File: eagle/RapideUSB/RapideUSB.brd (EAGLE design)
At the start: 50 x 50 mm, 36 parts, among them Y1 12-20MHz

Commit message: Board finished and ready to send to production.
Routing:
- net D3: track 62.4 -> 61.7 mm
- net GND: vias 19 -> 21
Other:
- board text added: "D+"
- board text added: "D+=D2"
- board text added: "D-"
- board text added: "D-=D4"
- board text added: "RapideUSB"
- board text added: "RapideUSB v1.0 Jan2015"
- board text added: "USB"
- board text added: "http://kalshagar.wikispaces.com/RapideUSB"
- board text removed: "C8"
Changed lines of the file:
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@@
 <text x="1.11125" y="42.06875" size="0.8128" layer="150" rot="R90">GND</text>
 <text x="1.11125" y="39.37" size="0.8128" layer="150" rot="R90">VCC</text>
-<text x="1.11125" y="30.95625" size="0.8128" layer="150" rot="R90">Cut  ok</text>
-<text x="50.00625" y="30.95625" size="0.8128" layer="150" rot="R90">Cut  ok</text>
+<text x="1.11125" y="30.95625" size="0.8128" layer="150" rot="R90">Cut ok</text>
+<text x="49.8475" y="30.95625" size="0.8128" layer="150" rot="R90">Cut ok</text>
 <rectangle x1="0" y1="17.78" x2="3.81" y2="20.32" layer="150"/>
 <text x="4.1275" y="7.46125" size="1.27" layer="150">ATtiny2313</text>
@@
 <text x="41.5925" y="15.71625" size="0.8128" layer="150">R2</text>
 <text x="41.5925" y="17.78" size="0.8128" layer="150">R3</text>
-<text x="1.27" y="25.4" size="1.27" layer="150">D0</text>
-<text x="26.67" y="25.4" size="1.27" layer="150">B328</text>
+<text x="1.27" y="25.7175" size="1.016" layer="150">D0</text>
+<text x="26.67" y="25.7175" size="1.016" layer="150">B328</text>
 <text x="23.65375" y="20.0025" size="0.8128" layer="150" rot="SR180">B2313</text>
-<text x="48.26" y="23.1775" size="0.8128" layer="150">C8</text>
 <text x="27.6225" y="21.74875" size="0.8128" layer="150">C0</text>
 <wire x1="20.32" y1="19.685" x2="17.145" y2="19.685" width="0.1524" layer="150"/>
@@
 <wire x1="33.655" y1="25.7175" x2="34.44875" y2="26.035" width="0.1524" layer="150"/>
 <text x="35.8775" y="16.35125" size="0.8128" layer="150">1.5k</text>
+<text x="48.73625" y="25.55875" size="1.27" layer="52" rot="MR0">http://kalshagar.wikispaces.com/RapideUSB</text>
+<text x="13.49375" y="25.55875" size="1.4224" layer="150">RapideUSB</text>
+<wire x1="20.32" y1="11.43" x2="16.51" y2="17.78" width="0.6096" layer="52"/>
+<wire x1="16.51" y1="17.78" x2="16.51" y2="11.43" width="0.6096" layer="52"/>
+<wire x1="16.51" y1="11.43" x2="16.51" y2="3.81" width="0.6096" layer="52"/>
+<wire x1="16.51" y1="3.81" x2="12.7" y2="11.43" width="0.6096" layer="52"/>
+<wire x1="16.51" y1="11.43" x2="19.05" y2="11.43" width="0.6096" layer="52"/>
+<wire x1="33.02" y1="6.35" x2="35.56" y2="10.16" width="0.6096" layer="150"/>
+<wire x1="35.56" y1="10.16" x2="35.56" y2="6.35" width="0.6096" layer="150"/>
+<wire x1="35.56" y1="6.35" x2="35.56" y2="2.54" width="0.6096" layer="150"/>
+<wire x1="35.56" y1="2.54" x2="38.1" y2="6.35" width="0.6096" layer="150"/>
+<wire x1="35.56" y1="6.35" x2="34.29" y2="6.35" width="0.6096" layer="150"/>
+<text x="14.2875" y="11.43" size="0.6096" layer="150" rot="R90">D+=D2</text>
+<text x="16.51" y="11.58875" size="0.6096" layer="150" rot="R90">D-=D4</text>
+<text x="13.0175" y="18.415" size="0.6096" layer="150">D+</text>
+<text x="15.5575" y="18.415" size="0.6096" layer="150">D-</text>
+<wire x1="3.81" y1="24.765" x2="3.81" y2="23.495" width="0.254" layer="150"/>
+<wire x1="21.59" y1="22.225" x2="21.59" y2="20.955" width="0.254" layer="150"/>
+<wire x1="29.21" y1="24.765" x2="29.21" y2="23.495" width="0.254" layer="150"/>
+<wire x1="31.75" y1="22.225" x2="31.75" y2="20.955" width="0.254" layer="150"/>
+<text x="20.0025" y="0.3175" size="0.6096" layer="150">RapideUSB v1.0 Jan2015</text>
+<text x="47.78375" y="8.41375" size="1.27" layer="150" rot="R90">USB</text>
 </plain>
 <attributes>
@@
 <wire x1="43.18" y1="12.54125" x2="44.1325" y2="10.795" width="0.4064" layer="1"/>
 <contactref element="C5" pad="2"/>
+<via x="3.81" y="5.08" extent="1-16" drill="0.5" shape="octagon"/>
+<via x="22.225" y="6.6675" extent="1-16" drill="0.5" shape="octagon"/>
 </signal>
 <signal name="B7">
@@
 <wire x1="30.1625" y1="3.4925" x2="31.115" y2="3.4925" width="0.1524" layer="16"/>
 <wire x1="30.1625" y1="7.3025" x2="30.1625" y2="3.4925" width="0.1524" layer="1"/>
-<wire x1="22.5425" y1="7.3025" x2="30.1625" y2="7.3025" width="0.1524" layer="1"/>
-<wire x1="20.32" y1="4.1275" x2="22.5425" y2="7.3025" width="0.1524" layer="1"/>
+<wire x1="25.0825" y1="7.3025" x2="30.1625" y2="7.3025" width="0.1524" layer="1"/>
+<wire x1="20.32" y1="4.1275" x2="25.0825" y2="7.3025" width="0.1524" layer="1"/>
 <wire x1="20.32" y1="2.54" x2="20.32" y2="4.1275" width="0.1524" layer="1"/>
 <wire x1="31.115" y1="3.4925" x2="31.2674" y2="3.55" width="0.1524" layer="16"/>

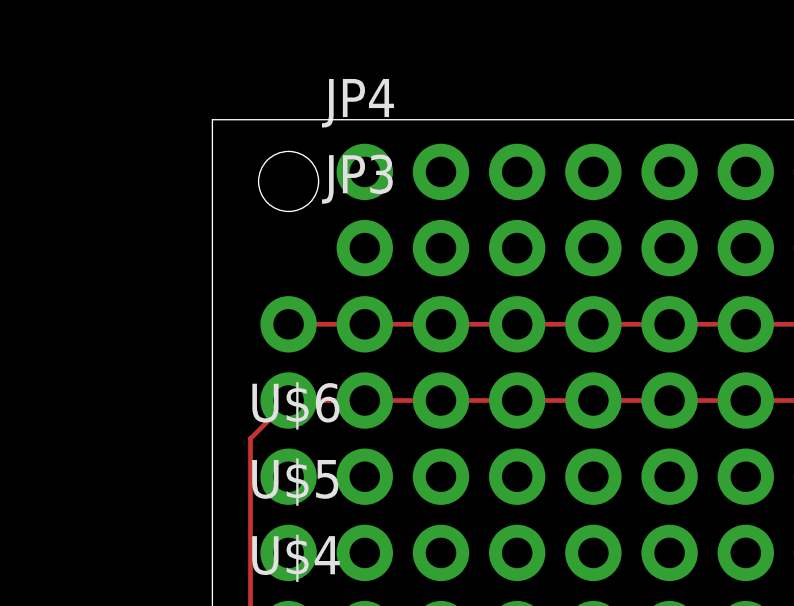
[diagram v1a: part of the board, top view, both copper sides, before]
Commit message: v1.1: fixed the power pin top-vias pins and added a nice V-USB logo.
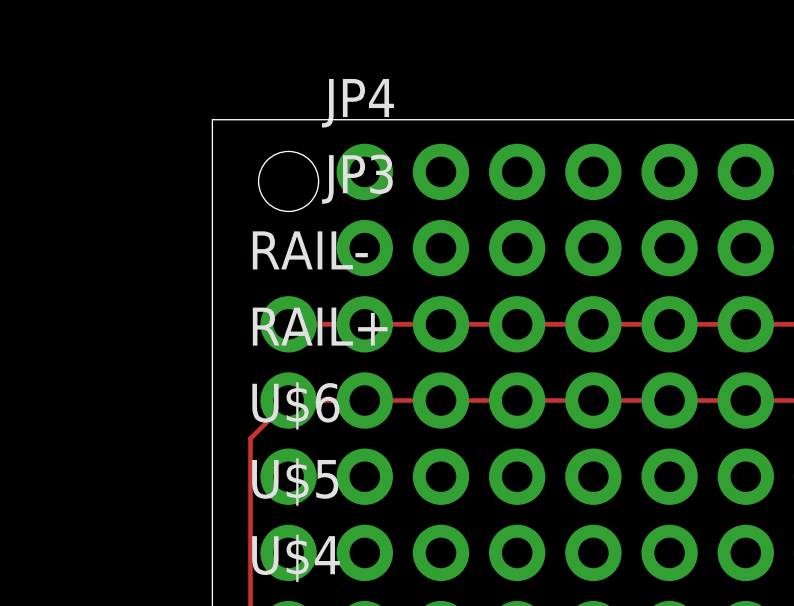
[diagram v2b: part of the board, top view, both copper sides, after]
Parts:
- added U$1: (no value), kalshagar-images:VUSB_LOGO
- RAIL+, RAIL-: value M17KIT -> M17NOSILK; device SparkFun-Connectors:1X17_NO_SILK_KIT -> SparkFun-Connectors:1X17_NO_SILK
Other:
- board text added: "RapideUSB v1.1 Jan2015"
- board text removed: "RapideUSB v1.0 Jan2015"
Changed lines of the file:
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@@
 <wire x1="29.21" y1="24.765" x2="29.21" y2="23.495" width="0.254" layer="150"/>
 <wire x1="31.75" y1="22.225" x2="31.75" y2="20.955" width="0.254" layer="150"/>
-<text x="20.0025" y="0.3175" size="0.6096" layer="150">RapideUSB v1.0 Jan2015</text>
+<text x="20.0025" y="0.3175" size="0.6096" layer="150">RapideUSB v1.1 Jan2015</text>
 <text x="47.78375" y="8.41375" size="1.27" layer="150" rot="R90">USB</text>
 </plain>
@@
 <element name="C3" library="resistor" package="C025-024X044" value="1uF" x="10.16" y="12.7"/>
 <element name="C4" library="resistor" package="E2-5" value="10uF+" x="10.16" y="16.51" rot="R90"/>
-<element name="RAIL+" library="SparkFun-Connectors" package="1X17_NO_SILK_KIT" value="M17KIT" x="2.54" y="40.64"/>
-<element name="RAIL-" library="SparkFun-Connectors" package="1X17_NO_SILK_KIT" value="M17KIT" x="2.54" y="43.18"/>
+<element name="RAIL+" library="SparkFun-Connectors" package="1X17_NO_SILK" value="M17NOSILK" x="2.54" y="40.64"/>
+<element name="RAIL-" library="SparkFun-Connectors" package="1X17_NO_SILK" value="M17NOSILK" x="2.54" y="43.18"/>
 <element name="U$2" library="SparkFun-Connectors" package="1X19_NO_SILK" value="M191X19_NO_SILK" x="2.54" y="27.94"/>
 <element name="U$3" library="SparkFun-Connectors" package="1X19_NO_SILK" value="M191X19_NO_SILK" x="2.54" y="30.48"/>
@@
 <element name="JP4" library="SparkFun-Connectors" package="1X16_NO_SILK" value="M161X16_NO_SILK" x="5.08" y="48.26"/>
 <element name="C5" library="resistor" package="C025-024X044" value="1uF" x="42.8625" y="1.74625" rot="R180"/>
+<element name="U$1" library="kalshagar-images" package="VUSB_LOGO" value="" x="32.385" y="12.3825"/>
 </elements>
 <signals>

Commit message: I made a mistake and PC2 is in fact not connected
Since I won't make another batch and that routing that one wire looks
like a nightmare, I just remove it from schematics to avoid confusion
later. A good lesson learnt.
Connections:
- removed net N$7: UC2.25
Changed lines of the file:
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@@
 <?xml version="1.0" encoding="utf-8"?>
 <!DOCTYPE eagle SYSTEM "eagle.dtd">
-<eagle version="6.3">
+<eagle version="7.2.0">
 <drawing>
 <settings>
@@
 <layer number="56" name="wert" color="7" fill="1" visible="no" active="no"/>
 <layer number="57" name="tCAD" color="7" fill="1" visible="no" active="no"/>
-<layer number="90" name="Modules" color="5" fill="1" visible="yes" active="yes"/>
+<layer number="90" name="Modules" color="5" fill="1" visible="no" active="no"/>
 <layer number="91" name="Nets" color="2" fill="1" visible="no" active="no"/>
 <layer number="92" name="Busses" color="1" fill="1" visible="no" active="no"/>
@@
 <pass name="Default">
 <param name="RoutingGrid" value="6.25mil"/>
+<param name="AutoGrid" value="1"/>
+<param name="Efforts" value="0"/>
+<param name="TopRouterVariant" value="1"/>
 <param name="tpViaShape" value="round"/>
 <param name="PrefDir.1" value="|"/>
@@
 <via x="35.2425" y="20.16125" extent="1-16" drill="0.3048"/>
 </signal>
-<signal name="N$7">
-<contactref element="UC2" pad="25"/>
-</signal>
 <signal name="N$8">

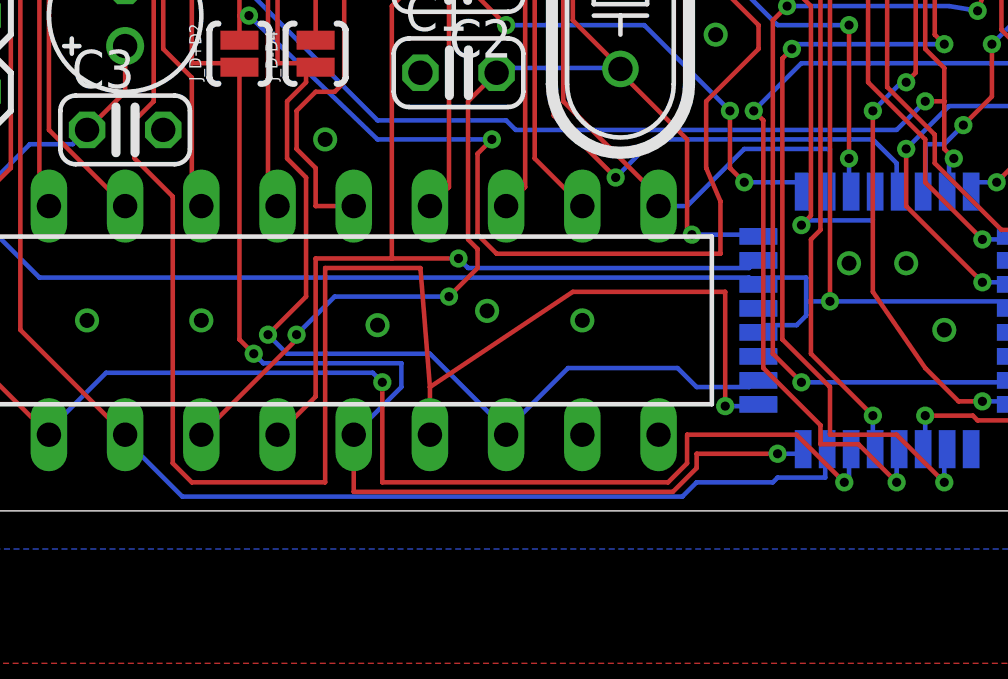
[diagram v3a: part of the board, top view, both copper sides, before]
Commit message: Bugfix: PD5 was unconnected on 2313
Added missing wire on board v1.2.
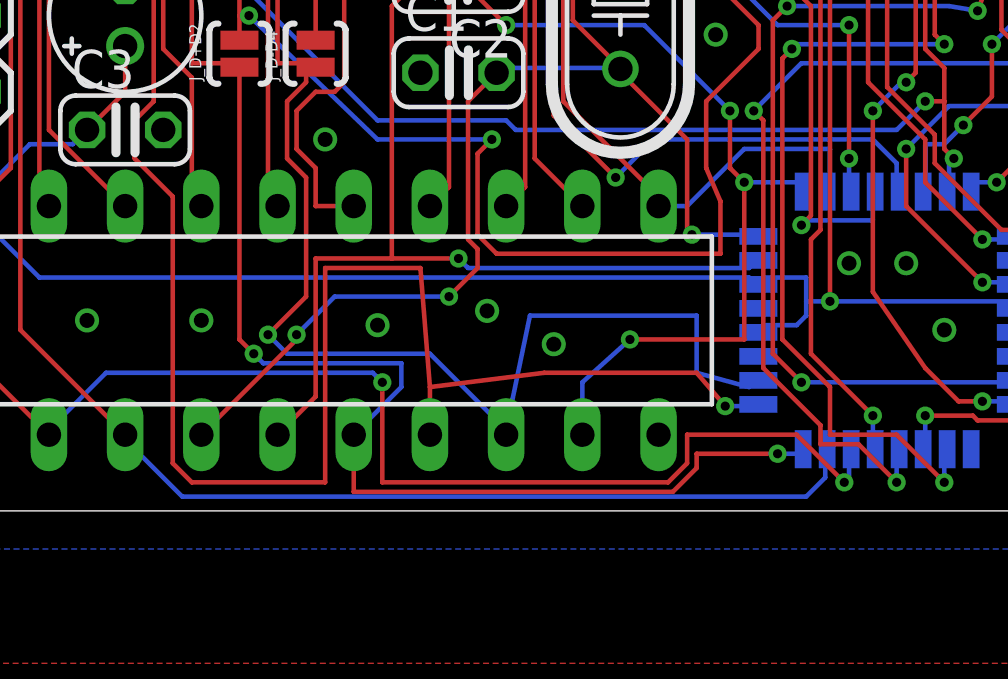
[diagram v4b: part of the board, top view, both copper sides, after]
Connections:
- removed net N$16: PORTD.6, UC2.9
- net D5: now also PORTD.6, UC2.9
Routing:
- net D5: track 0.00 -> 39.1 mm, vias 0 -> 4
- net N$16: track 26.2 -> 0.00 mm, vias 3 -> 0
- net D3: track 61.7 -> 57.5 mm
- net D4: track 41.1 -> 45.1 mm
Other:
- board text added: "RapideUSB v1.2 Dec2016"
- board text added: "http://electrogeek.cc/RapideUSB"
- board text removed: "RapideUSB v1.1 Jan2015"
- board text removed: "http://kalshagar.wikispaces.com/RapideUSB"
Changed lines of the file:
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@@
 <wire x1="33.655" y1="25.7175" x2="34.44875" y2="26.035" width="0.1524" layer="150"/>
 <text x="35.8775" y="16.35125" size="0.8128" layer="150">1.5k</text>
-<text x="48.73625" y="25.55875" size="1.27" layer="52" rot="MR0">http://kalshagar.wikispaces.com/RapideUSB</text>
+<text x="48.73625" y="25.55875" size="1.27" layer="52" rot="MR0">http://electrogeek.cc/RapideUSB</text>
 <text x="13.49375" y="25.55875" size="1.4224" layer="150">RapideUSB</text>
 <wire x1="20.32" y1="11.43" x2="16.51" y2="17.78" width="0.6096" layer="52"/>
@@
 <wire x1="29.21" y1="24.765" x2="29.21" y2="23.495" width="0.254" layer="150"/>
 <wire x1="31.75" y1="22.225" x2="31.75" y2="20.955" width="0.254" layer="150"/>
-<text x="20.0025" y="0.3175" size="0.6096" layer="150">RapideUSB v1.1 Jan2015</text>
+<text x="20.0025" y="0.3175" size="0.6096" layer="150">RapideUSB v1.2 Dec2016</text>
 <text x="47.78375" y="8.41375" size="1.27" layer="150" rot="R90">USB</text>
 </plain>
@@
 <via x="16.8275" y="12.3825" extent="1-16" drill="0.5" shape="octagon"/>
 <via x="18.7325" y="18.7325" extent="1-16" drill="0.5" shape="octagon"/>
-<via x="25.4" y="6.35" extent="1-16" drill="0.5" shape="octagon"/>
+<via x="24.4475" y="5.55625" extent="1-16" drill="0.5" shape="octagon"/>
 <via x="34.29" y="8.255" extent="1-16" drill="0.5" shape="octagon"/>
 <via x="37.465" y="6.0325" extent="1-16" drill="0.5" shape="octagon"/>
@@
 <contactref element="PORTD" pad="5"/>
 <wire x1="30.95625" y1="4.1275" x2="31.115" y2="4.28625" width="0.1524" layer="16"/>
-<wire x1="29.21" y1="4.1275" x2="30.95625" y2="4.1275" width="0.1524" layer="16"/>
-<wire x1="28.575" y1="4.7625" x2="29.21" y2="4.1275" width="0.1524" layer="16"/>
-<wire x1="24.92375" y1="4.7625" x2="28.575" y2="4.7625" width="0.1524" layer="16"/>
-<wire x1="22.86" y1="2.69875" x2="24.92375" y2="4.7625" width="0.1524" layer="16"/>
+<wire x1="29.21" y1="4.60375" x2="30.95625" y2="4.1275" width="0.1524" layer="16"/>
+<wire x1="29.21" y1="6.50875" x2="29.21" y2="4.60375" width="0.1524" layer="16"/>
+<wire x1="23.65375" y1="6.50875" x2="29.21" y2="6.50875" width="0.1524" layer="16"/>
+<wire x1="22.86" y1="2.69875" x2="23.65375" y2="6.50875" width="0.1524" layer="16"/>
 <wire x1="31.115" y1="4.28625" x2="31.2674" y2="4.35" width="0.1524" layer="16"/>
 <wire x1="15.24" y1="14.9225" x2="16.1925" y2="14.9225" width="0.1524" layer="1"/>
@@
 <via x="42.545" y="3.4925" extent="1-16" drill="0.3048"/>
 </signal>
-<signal name="N$16">
-<contactref element="UC2" pad="9"/>
-<contactref element="PORTD" pad="6"/>
-<wire x1="32.54375" y1="10.95375" x2="32.7025" y2="10.795" width="0.1524" layer="16"/>
-<wire x1="30.7975" y1="10.95375" x2="32.54375" y2="10.95375" width="0.1524" layer="16"/>
-<wire x1="30.32125" y1="11.43" x2="30.7975" y2="10.95375" width="0.1524" layer="1"/>
-<wire x1="30.32125" y1="13.335" x2="30.32125" y2="11.43" width="0.1524" layer="1"/>
-<wire x1="27.46375" y1="16.1925" x2="30.32125" y2="13.335" width="0.1524" layer="16"/>
-<wire x1="22.86" y1="16.1925" x2="27.46375" y2="16.1925" width="0.1524" layer="16"/>
-<wire x1="21.2725" y1="17.78" x2="22.86" y2="16.1925" width="0.1524" layer="1"/>
-<wire x1="21.2725" y1="18.89125" x2="21.2725" y2="17.78" width="0.1524" layer="1"/>
-<wire x1="19.05" y1="21.11375" x2="21.2725" y2="18.89125" width="0.1524" layer="1"/>
-<wire x1="19.05" y1="22.06625" x2="19.05" y2="21.11375" width="0.1524" layer="1"/>
-<wire x1="18.25625" y1="22.86" x2="19.05" y2="22.06625" width="0.1524" layer="1"/>
-<wire x1="15.24" y1="22.86" x2="18.25625" y2="22.86" width="0.1524" layer="1"/>
-<wire x1="15.24" y1="24.13" x2="15.24" y2="22.86" width="0.1524" layer="1"/>
-<wire x1="32.7025" y1="10.795" x2="32.76" y2="10.6426" width="0.1524" layer="16"/>
-<via x="30.7975" y="10.95375" extent="1-16" drill="0.3048"/>
-<via x="30.32125" y="13.335" extent="1-16" drill="0.3048"/>
-<via x="22.86" y="16.1925" extent="1-16" drill="0.3048"/>
-</signal>
 <signal name="D7">
 <contactref element="UC2" pad="11"/>
@@
 <signal name="D5">
 <contactref element="UC1" pad="9"/>
+<contactref element="UC2" pad="9"/>
+<contactref element="PORTD" pad="6"/>
+<wire x1="32.54375" y1="10.95375" x2="32.7025" y2="10.795" width="0.1524" layer="16"/>
+<wire x1="30.7975" y1="10.95375" x2="32.54375" y2="10.95375" width="0.1524" layer="16"/>
+<wire x1="30.32125" y1="11.43" x2="30.7975" y2="10.95375" width="0.1524" layer="1"/>
+<wire x1="30.32125" y1="13.335" x2="30.32125" y2="11.43" width="0.1524" layer="1"/>
+<wire x1="27.46375" y1="16.1925" x2="30.32125" y2="13.335" width="0.1524" layer="16"/>
+<wire x1="22.86" y1="16.1925" x2="27.46375" y2="16.1925" width="0.1524" layer="16"/>
+<wire x1="21.2725" y1="17.78" x2="22.86" y2="16.1925" width="0.1524" layer="1"/>
+<wire x1="21.2725" y1="18.89125" x2="21.2725" y2="17.78" width="0.1524" layer="1"/>
+<wire x1="19.05" y1="21.11375" x2="21.2725" y2="18.89125" width="0.1524" layer="1"/>
+<wire x1="19.05" y1="22.06625" x2="19.05" y2="21.11375" width="0.1524" layer="1"/>
+<wire x1="18.25625" y1="22.86" x2="19.05" y2="22.06625" width="0.1524" layer="1"/>
+<wire x1="15.24" y1="22.86" x2="18.25625" y2="22.86" width="0.1524" layer="1"/>
+<wire x1="15.24" y1="24.13" x2="15.24" y2="22.86" width="0.1524" layer="1"/>
+<wire x1="32.7025" y1="10.795" x2="32.76" y2="10.6426" width="0.1524" layer="16"/>
+<via x="30.7975" y="10.95375" extent="1-16" drill="0.3048"/>
+<via x="30.32125" y="13.335" extent="1-16" drill="0.3048"/>
+<via x="22.86" y="16.1925" extent="1-16" drill="0.3048"/>
+<wire x1="30.7975" y1="10.95375" x2="30.7975" y2="5.715" width="0.1524" layer="1"/>
+<wire x1="30.7975" y1="5.715" x2="26.9875" y2="5.715" width="0.1524" layer="1"/>
+<wire x1="26.9875" y1="5.715" x2="25.4" y2="4.28625" width="0.1524" layer="16"/>
+<wire x1="25.4" y1="4.28625" x2="25.4" y2="2.54" width="0.1524" layer="16"/>
+<via x="26.9875" y="5.715" extent="1-16" drill="0.3048"/>
 </signal>
 <signal name="D3">
@@
 <contactref element="PORTD" pad="4"/>
 <wire x1="30.1625" y1="3.4925" x2="31.115" y2="3.4925" width="0.1524" layer="16"/>
-<wire x1="30.1625" y1="7.3025" x2="30.1625" y2="3.4925" width="0.1524" layer="1"/>
-<wire x1="25.0825" y1="7.3025" x2="30.1625" y2="7.3025" width="0.1524" layer="1"/>
-<wire x1="20.32" y1="4.1275" x2="25.0825" y2="7.3025" width="0.1524" layer="1"/>
+<wire x1="29.21" y1="4.60375" x2="30.1625" y2="3.4925" width="0.1524" layer="1"/>
+<wire x1="24.13" y1="4.60375" x2="29.21" y2="4.60375" width="0.1524" layer="1"/>
+<wire x1="20.32" y1="4.1275" x2="24.13" y2="4.60375" width="0.1524" layer="1"/>
 <wire x1="20.32" y1="2.54" x2="20.32" y2="4.1275" width="0.1524" layer="1"/>
 <wire x1="31.115" y1="3.4925" x2="31.2674" y2="3.55" width="0.1524" layer="16"/>
@@
 <contactref element="PORTD" pad="2"/>
 <wire x1="33.49625" y1="1.11125" x2="33.49625" y2="1.905" width="0.1524" layer="16"/>
-<wire x1="31.90875" y1="1.11125" x2="33.49625" y2="1.11125" width="0.1524" layer="16"/>
-<wire x1="31.75" y1="0.9525" x2="31.90875" y2="1.11125" width="0.1524" layer="16"/>
-<wire x1="29.21" y1="0.9525" x2="31.75" y2="0.9525" width="0.1524" layer="16"/>
-<wire x1="28.73375" y1="0.47625" x2="29.21" y2="0.9525" width="0.1524" layer="16"/>
-<wire x1="12.065" y1="0.47625" x2="28.73375" y2="0.47625" width="0.1524" layer="16"/>
+<wire x1="32.86125" y1="0.47625" x2="33.49625" y2="1.11125" width="0.1524" layer="16"/>
+<wire x1="12.065" y1="0.47625" x2="32.86125" y2="0.47625" width="0.1524" layer="16"/>
 <wire x1="10.16" y1="2.38125" x2="12.065" y2="0.47625" width="0.1524" layer="16"/>
 <wire x1="10.16" y1="2.54" x2="10.16" y2="2.38125" width="0.1524" layer="16"/>
